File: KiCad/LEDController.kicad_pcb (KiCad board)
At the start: 4 copper layers, 90 x 90 mm, 86 parts, among them J1 UART, J10 LED2, J13 LED3, J14 LED4, J15 LED8, J16 LED7, J17 LED6, J18 LED5, J19 LED9, J20 LED10, J21 LED11, J22 LED12, J4 Conn_01x02, J5 Conn_01x02, J6 USB_C_Receptacle_USB2.0_16P, J7 Conn_01x14, J8 JTAG, J9 LED1, K1 SRD-05VDC-SL-C, Q5 AO3400A, SW1 BOOT, SW2 EN, U1 TPS54202DDC, U2 ESP32-S3-WROOM-2, U3 TPS54202DDC, U7 SN74LVC8T245, U8 SN74LVC8T245

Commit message: arrange components
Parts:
- J10, J13, J14, J15, J16, J17, J18, J19, J20, J21, J22, J9: footprint TerminalBlock_Phoenix:TerminalBlock_Phoenix_MKDS-3-3-5.08_1x03_P5.08mm_Horizontal -> Library:CONN-TH_3P-P5.08_WJ2EDGRC-5.08-3P
- J4: value Conn_01x02 -> 5V; footprint TerminalBlock_Phoenix:TerminalBlock_Phoenix_MKDS-3-2-5.08_1x02_P5.08mm_Horizontal -> Library:CONN-TH_HB9500M-9.5-2P
- J5: value Conn_01x02 -> 24V; footprint TerminalBlock_Phoenix:TerminalBlock_Phoenix_MKDS-3-2-5.08_1x02_P5.08mm_Horizontal -> Library:CONN-TH_HB9500M-9.5-2P
- moved H2 113.6 mm to (127.0, 52.0)
- moved D3 69.8 mm to (173.8, 86.0)
- moved R13 69.8 mm to (174.0, 80.0)
- moved R14 69.8 mm to (174.0, 83.0)
- moved H1 62.9 mm to (48.0, 52.0)
- moved J6 62.6 mm to (105.0, 52.7)
- moved C22 49.7 mm to (85.4, 136.8)
- moved C23 49.7 mm to (79.4, 136.8)
- moved C24 49.7 mm to (89.9, 122.8)
- moved C25 49.7 mm to (95.9, 122.8)
- moved R35 49.7 mm to (75.4, 136.3)
- moved R36 49.7 mm to (75.4, 134.3)
- moved R37 49.7 mm to (75.4, 132.3)
- moved R38 49.7 mm to (75.4, 130.3)
- moved R39 49.7 mm to (75.4, 128.3)
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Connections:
- D3 pad 1: +24V -> +5V
- J4 pad 1: +24V -> +5V
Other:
- board size 90 x 90 mm -> 85 x 110 mm
- board text removed: "-"
- board text removed: "RX"
- board text removed: "TX"

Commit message: arrange  components
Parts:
- removed J21: LED11, Library:CONN-TH_3P-P5.08_WJ2EDGRC-5.08-3P
- removed J22: LED12, Library:CONN-TH_3P-P5.08_WJ2EDGRC-5.08-3P
- removed R45, R46: 100, Resistor_SMD:R_0805_2012Metric_Pad1.20x1.40mm_HandSolder
- moved D1 51.8 mm to (209.4, 57.8)
- moved R5 51.7 mm to (204.9, 58.0), turned to 0 degrees
- moved R8 48.3 mm to (204.9, 63.9)
- moved R6 48.2 mm to (204.9, 60.9), turned to 0 degrees
- moved J20 32.2 mm to (119.5, 88.1)
- moved J19 30.8 mm to (119.5, 107.0)
- moved R35 28.5 mm to (99.8, 121.5), turned to 0 degrees
- moved J7 26.8 mm to (179.8, 58.8)
- moved R36 26.7 mm to (99.8, 123.5), turned to 0 degrees
- moved C21 26.6 mm to (95.2, 104.6), turned to 180 degrees
- moved R37 25.3 mm to (99.8, 125.5), turned to 0 degrees
- moved R12 24.8 mm to (108.8, 78.1), turned to 0 degrees
- moved J15 23.1 mm to (119.5, 126.0), turned to 90 degrees
- moved R11 21.3 mm to (104.7, 78.1), turned to 0 degrees
- moved R20 21.0 mm to (104.8, 94.5), turned to 0 degrees
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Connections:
- R35 pad 1: Net-(U7-B1) -> Net-(U8-B6)
- R35 pad 2: DataOut1 -> DataOut8
- R36 pad 1: Net-(U7-B2) -> Net-(U8-B7)
- R36 pad 2: DataOut2 -> DataOut7
- R37 pad 1: Net-(U7-B3) -> Net-(U8-B8)
- R37 pad 2: DataOut3 -> DataOut6
- R38 pad 2: DataOut4 -> DataOut5
- R39 pad 2: DataOut5 -> DataOut4
- R40 pad 2: DataOut6 -> DataOut3
- R41 pad 2: DataOut7 -> DataOut2
- R42 pad 2: DataOut8 -> DataOut1
- R43 pad 1: Net-(U8-B1) -> Net-(U8-B5)
- R44 pad 1: Net-(U8-B2) -> Net-(U8-B4)
- U7 pad 10: Data8 -> Data1
- U7 pad 19: Net-(U7-B3) -> unconnected-(U7-B3-Pad19)
- U7 pad 20: Net-(U7-B2) -> unconnected-(U7-B2-Pad20)
- U7 pad 21: Net-(U7-B1) -> unconnected-(U7-B1-Pad21)
- U7 pad 3: Data1 -> unconnected-(U7-A1-Pad3)
- U7 pad 4: Data2 -> unconnected-(U7-A2-Pad4)
- U7 pad 5: Data3 -> unconnected-(U7-A3-Pad5)
- U7 pad 6: Data4 -> Data5
- U7 pad 7: Data5 -> Data4
- U7 pad 8: Data6 -> Data3
- U7 pad 9: Data7 -> Data2
- U8 pad 10: unconnected-(U8-A8-Pad10) -> Data6
- U8 pad 14: unconnected-(U8-B8-Pad14) -> Net-(U8-B8)
- U8 pad 15: unconnected-(U8-B7-Pad15) -> Net-(U8-B7)
- U8 pad 16: unconnected-(U8-B6-Pad16) -> Net-(U8-B6)
- U8 pad 17: unconnected-(U8-B5-Pad17) -> Net-(U8-B5)
- U8 pad 19: Net-(U8-B3) -> unconnected-(U8-B3-Pad19)
- U8 pad 20: Net-(U8-B2) -> unconnected-(U8-B2-Pad20)
- U8 pad 21: Net-(U8-B1) -> unconnected-(U8-B1-Pad21)
- U8 pad 3: Data9 -> unconnected-(U8-A1-Pad3)
- U8 pad 4: Data10 -> unconnected-(U8-A2-Pad4)
- U8 pad 5: Data11 -> unconnected-(U8-A3-Pad5)
- U8 pad 6: Data12 -> Data10
- U8 pad 7: unconnected-(U8-A5-Pad7) -> Data9
- U8 pad 8: unconnected-(U8-A6-Pad8) -> Data8
- U8 pad 9: unconnected-(U8-A7-Pad9) -> Data7
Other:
- board size 85 x 110 mm -> 85 x 100 mm
- board text removed: "3V3"
- board text removed: "G11"
- board text removed: "G12"
- board text removed: "G13"
- board text removed: "G14"
- board text removed: "G17"
- board text removed: "G18"
- board text removed: "G21"
- board text removed: "G38"
- board text removed: "G45"
- board text removed: "G46"
- board text removed: "G47"
- board text removed: "G8"
- board text removed: "GND"

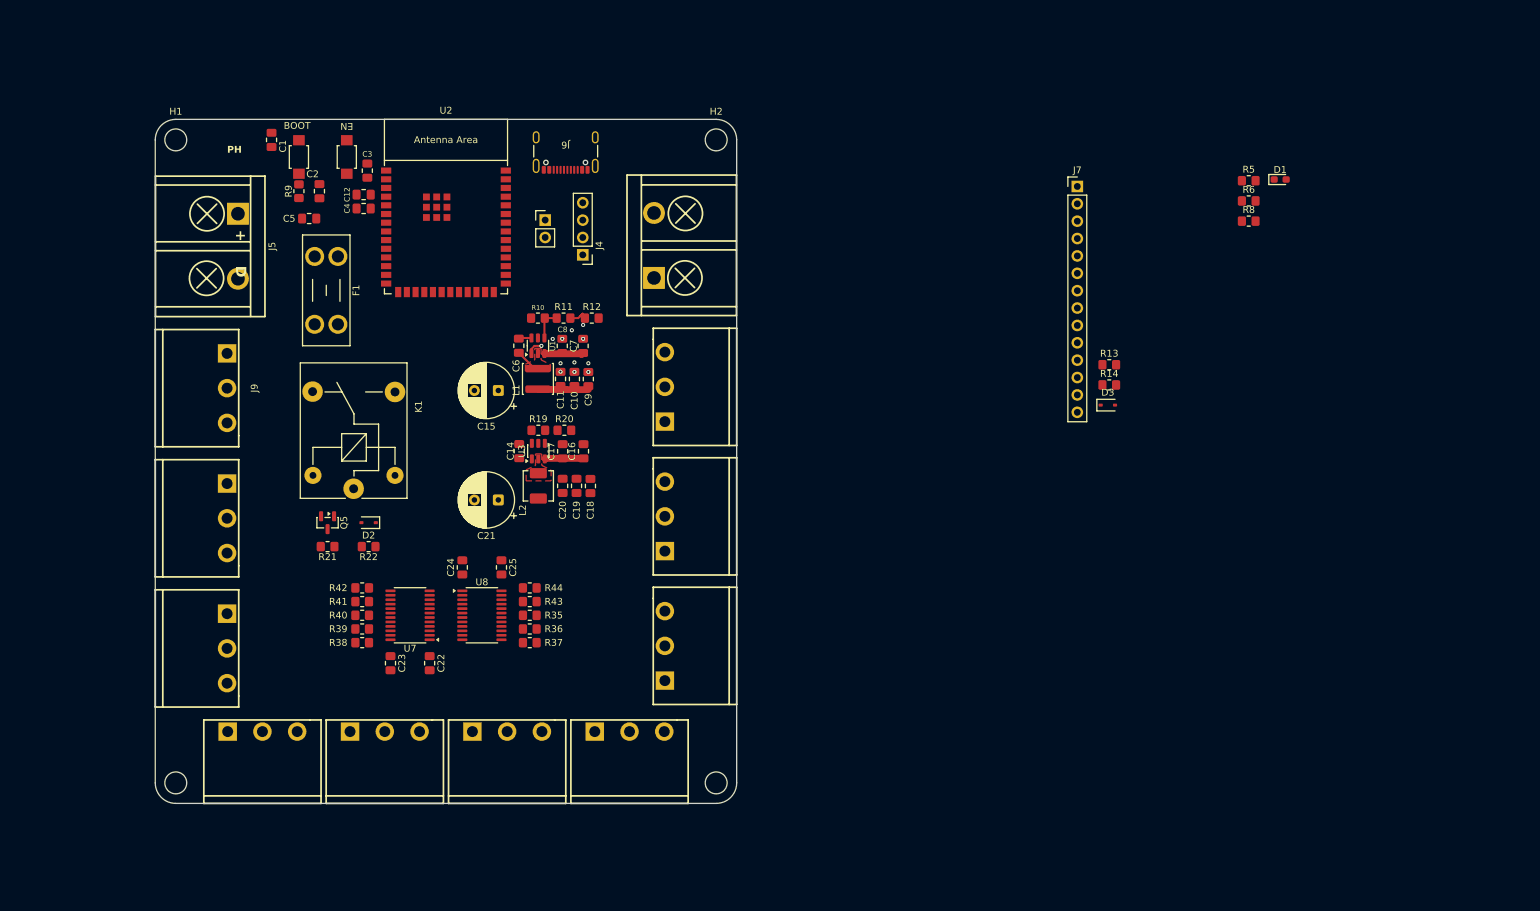
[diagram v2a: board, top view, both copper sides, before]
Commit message: add ideal diode
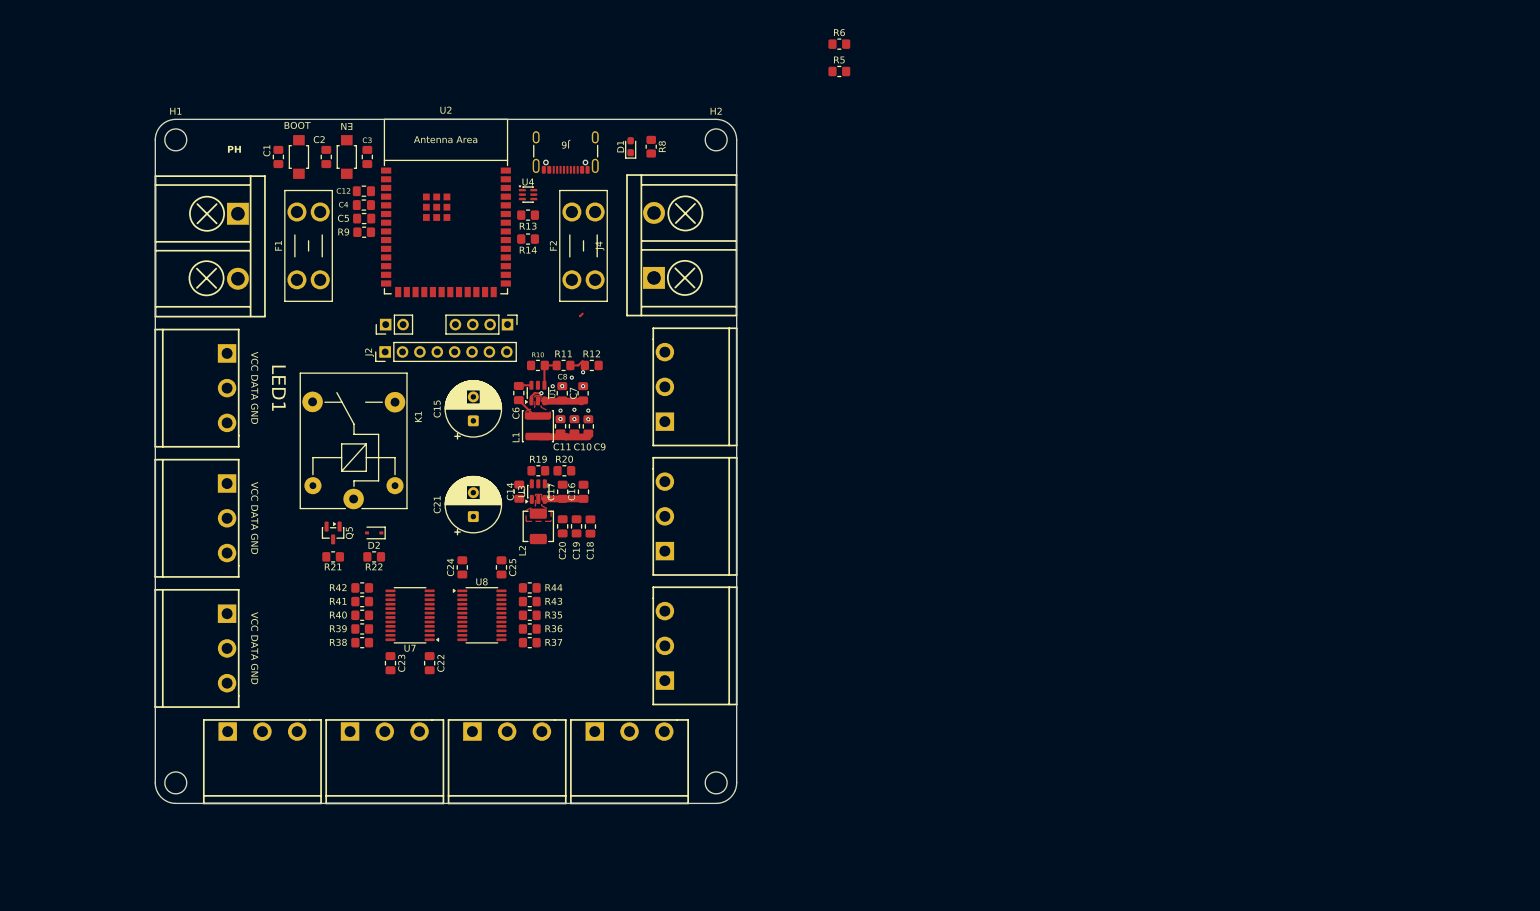
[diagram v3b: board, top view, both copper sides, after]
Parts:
- removed D3: 1N4148WS, Diode_SMD:D_SOD-323
- removed J7: Conn_01x14, Connector_PinHeader_2.54mm:PinHeader_1x14_P2.54mm_Vertical
- added F2: Fuse, Fuse:Fuseholder_Blade_Mini_Keystone_3568, F.Cu at (105.9, 72.5)
- added J2: Conn_01x08, Connector_PinHeader_2.54mm:PinHeader_1x08_P2.54mm_Vertical, F.Cu at (78.6, 83.0)
- added U4: LM66100DCK, Package_TO_SOT_SMD:SOT-363_SC-70-6, F.Cu at (99.5, 60.0)
- moved D1 95.1 mm to (114.5, 53.0), turned to 90 degrees
- moved R8 88.0 mm to (117.5, 53.0), turned to -90 degrees
- moved R13 87.7 mm to (99.5, 63.0), turned to 180 degrees
- moved R14 87.6 mm to (99.5, 66.5), turned to 180 degrees
- moved R6 64.1 mm to (145.0, 38.0)
- moved R5 62.0 mm to (145.0, 42.0)
- moved J1 27.9 mm to (78.7, 79.0), turned to 90 degrees
- moved J8 15.0 mm to (96.5, 79.0), turned to -90 degrees
- moved R9 11.3 mm to (75.5, 65.5), turned to 0 degrees
- moved C5 8.04 mm to (75.5, 63.5)
- moved C10 6.92 mm to (106.3, 93.9)
- moved C11 6.92 mm to (104.2, 93.9)
- moved C9 6.92 mm to (108.3, 93.9)
- moved L1 6.92 mm to (100.9, 93.9)
- moved R10 6.92 mm to (100.9, 85.0)
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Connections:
- F1 pad 2: Net-(F1-Pad2) -> Net-(J5-Pin_1)
- J4 pad 1: +5V -> Net-(J4-Pin_1)
- J5 pad 1: +24V -> Net-(J5-Pin_1)
- K1 pad 1: Net-(F1-Pad2) -> +24V
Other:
- board text added: "LED1"
- board text added: "VCC DATA GND"
- board text removed: "+"
- board text removed: "D"

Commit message: add esd protection, pullup on EN, Replicate layout
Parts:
- removed L1: 10u, Inductor_SMD:L_APV_ANR4026
- added C26: 220uF, Capacitor_THT:CP_Radial_D8.0mm_P3.50mm, F.Cu at (103.3, 93.0)
- added C27: 75p, Capacitor_SMD:C_0805_2012Metric_Pad1.18x1.45mm_HandSolder, F.Cu at (83.2, 111.0)
- added J3: Power over USB, Connector_PinHeader_2.54mm:PinHeader_1x02_P2.54mm_Vertical, F.Cu at (106.7, 84.5)
- added L3: 15u, Inductor_SMD:L_APV_APH0630, F.Cu at (96.0, 97.5)
- added R15: 22, Resistor_SMD:R_0805_2012Metric_Pad1.20x1.40mm_HandSolder, F.Cu at (75.5, 71.5)
- added R7: 22, Resistor_SMD:R_0805_2012Metric_Pad1.20x1.40mm_HandSolder, F.Cu at (75.5, 73.5)
- added U5: USBLC6-2SC6, Package_TO_SOT_SMD:SOT-23-6, F.Cu at (100.5, 61.0)
- C15: value 220uF -> 56p; footprint Capacitor_THT:CP_Radial_D8.0mm_P3.50mm -> Capacitor_SMD:C_0805_2012Metric_Pad1.18x1.45mm_HandSolder
- L2: footprint Inductor_SMD:L_APV_APH0420 -> Inductor_SMD:L_APV_APH0630
- R11: value 1.8k -> 10k
- R12: value 20k -> 22k
- moved R8 53.4 mm to (71.8, 80.5)
- moved D1 52.5 mm to (69.8, 80.5)
- moved R12 24.6 mm to (85.5, 92.8), turned to 90 degrees
- moved R14 21.7 mm to (116.5, 53.0), turned to -90 degrees
- moved R20 20.2 mm to (85.5, 106.3), turned to 90 degrees
- moved R10 19.9 mm to (85.5, 97.5), turned to 90 degrees
- moved R19 18.8 mm to (85.5, 111.0), turned to 90 degrees
- moved C7 18.7 mm to (89.0, 91.8), turned to 180 degrees
- moved C16 18.7 mm to (89.0, 105.3), turned to 180 degrees
- moved R13 17.8 mm to (114.2, 53.0), turned to -90 degrees
- moved C8 16.2 mm to (89.0, 93.9), turned to 180 degrees
- moved C17 16.0 mm to (89.0, 107.4), turned to 180 degrees
- moved C18 15.7 mm to (93.8, 103.3), turned to 180 degrees
- moved C6 15.0 mm to (89.0, 100.8), turned to 180 degrees
- moved U1 14.7 mm to (89.0, 97.5), turned to 180 degrees
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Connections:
- net +24V renamed VCC_IN
- net +24V_SW renamed VCC_SW
- C15 pad 2: GND -> Net-(U1-FB)
- J6 pad A6: USB.D+ -> Net-(J6-D+-PadA6)
- J6 pad A7: USB.D- -> Net-(J6-D--PadA7)
- J6 pad B6: USB.D+ -> Net-(J6-D+-PadA6)
- J6 pad B7: USB.D- -> Net-(J6-D--PadA7)
- R11 pad 1: Net-(U1-FB) -> +3.3V
- R11 pad 2: Net-(R11-Pad2) -> ESP_BOOT
- R12 pad 1: Net-(R11-Pad2) -> Net-(U1-FB)
- R13 pad 1: Net-(J6-CC1) -> GND
- R13 pad 2: GND -> Net-(J6-CC2)
- R14 pad 1: Net-(J6-CC2) -> GND
- R14 pad 2: GND -> Net-(J6-CC1)
- R35 pad 1: Net-(U8-B6) -> Net-(U8-B4)
- R36 pad 1: Net-(U8-B7) -> Net-(U8-B6)
- R38 pad 1: Net-(U7-B4) -> Net-(U7-B1)
- R39 pad 1: Net-(U7-B5) -> Net-(U7-B3)
- R40 pad 1: Net-(U7-B6) -> Net-(U7-B5)
- R43 pad 1: Net-(U8-B5) -> Net-(U8-B2)
- R44 pad 1: Net-(U8-B4) -> Net-(U8-B1)
- U2 pad 13: USB.D- -> Net-(U2-GPIO19/U1RTS/ADC2_CH8/CLK_OUT2/USB_D-)
- U2 pad 14: USB.D+ -> Net-(U2-GPIO20/U1CTS/ADC2_CH9/CLK_OUT1/USB_D+)
- U7 pad 16: Net-(U7-B6) -> unconnected-(U7-B6-Pad16)
- U7 pad 18: Net-(U7-B4) -> unconnected-(U7-B4-Pad18)
- U7 pad 19: unconnected-(U7-B3-Pad19) -> Net-(U7-B3)
- U7 pad 21: unconnected-(U7-B1-Pad21) -> Net-(U7-B1)
- U7 pad 3: unconnected-(U7-A1-Pad3) -> Data5
- U7 pad 5: unconnected-(U7-A3-Pad5) -> Data4
- U7 pad 6: Data5 -> unconnected-(U7-A4-Pad6)
- U7 pad 7: Data4 -> Data3
- U7 pad 8: Data3 -> unconnected-(U7-A6-Pad8)
- U8 pad 15: Net-(U8-B7) -> unconnected-(U8-B7-Pad15)
- U8 pad 17: Net-(U8-B5) -> unconnected-(U8-B5-Pad17)
- U8 pad 20: unconnected-(U8-B2-Pad20) -> Net-(U8-B2)
- U8 pad 21: unconnected-(U8-B1-Pad21) -> Net-(U8-B1)
- U8 pad 3: unconnected-(U8-A1-Pad3) -> Data10
- U8 pad 4: unconnected-(U8-A2-Pad4) -> Data9
- U8 pad 6: Data10 -> Data8
- U8 pad 7: Data9 -> unconnected-(U8-A5-Pad7)
- U8 pad 8: Data8 -> Data7
- U8 pad 9: Data7 -> unconnected-(U8-A7-Pad9)
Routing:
- net +5V: track 0.00 -> 14.5 mm
- net VCC_IN: track 12.1 -> 4.21 mm
- net Net-(U3-FB): track 0.00 -> 7.31 mm
- net +3.3V: track 7.31 -> 14.5 mm
- net Net-(U3-SW): track 0.00 -> 4.57 mm
- net Net-(U1-FB): track 4.60 -> 7.31 mm
- net Net-(R11-Pad2): track 2.59 -> 0.00 mm
- net Net-(U3-BOOT): track 0.00 -> 2.43 mm
- net GND: track 2.31 -> 0.00 mm, vias 12 -> 0
- net Net-(U1-SW): track 3.24 -> 4.57 mm
- net Net-(U1-BOOT): track 1.74 -> 2.43 mm
- added copper zone on F.Cu, net GND
- added copper zone on In1.Cu, net GND
- added copper zone on In2.Cu, net GND
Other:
- board text added: "Close for Power over USB Open for ext. PSU"
- board text added: "LED2"
- board text added: "LED3"
- board text added: "LED4"
- board text added: "LED5"
- board text added: "LED6"
- board text added: "LED7"

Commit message: cleanup kicad folder
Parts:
- moved R6 57.9 mm to (100.5, 75.0), turned to 180 degrees
- moved R5 56.6 mm to (100.5, 77.0), turned to 180 degrees
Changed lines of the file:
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@@
 	(footprint "Resistor_SMD:R_0805_2012Metric_Pad1.20x1.40mm_HandSolder"
 		(layer "F.Cu")
-		(at 145 38)
+		(at 100.5 75 180)
 		(descr "Resistor SMD 0805 (2012 Metric), square (rectangular) end terminal, IPC-7351 nominal with elongated pad for handsoldering. (Body size source: IPC-SM-782 page 72, https://www.pcb-3d.com/wordpress/wp-content/uploads/ipc-sm-782a_amendment_1_and_2.pdf)")
 		(tags "resistor handsolder")
@@
 		)
 		(property "LCSC" "C2930231"
-			(at 0 0 0)
+			(at 0 0 180)
 			(unlocked yes)
 			(layer "F.Fab")
@@
 		(duplicate_pad_numbers_are_jumpers no)
 		(fp_line
-			(start -0.227064 -0.735)
-			(end 0.227064 -0.735)
+			(start -0.227064 0.735)
+			(end 0.227064 0.735)
 			(stroke
 				(width 0.12)
@@
 		)
 		(fp_line
-			(start -0.227064 0.735)
-			(end 0.227064 0.735)
+			(start -0.227064 -0.735)
+			(end 0.227064 -0.735)
 			(stroke
 				(width 0.12)
@@
 		)
 		(pad "1" smd roundrect
-			(at -1 0)
+			(at -1 0 180)
 			(size 1.2 1.4)
 			(layers "F.Cu" "F.Mask" "F.Paste")
@@
 		)
 		(pad "2" smd roundrect
-			(at 1 0)
+			(at 1 0 180)
 			(size 1.2 1.4)
 			(layers "F.Cu" "F.Mask" "F.Paste")
@@
 	(footprint "Resistor_SMD:R_0805_2012Metric_Pad1.20x1.40mm_HandSolder"
 		(layer "F.Cu")
-		(at 145 42)
+		(at 100.5 77 180)
 		(descr "Resistor SMD 0805 (2012 Metric), square (rectangular) end terminal, IPC-7351 nominal with elongated pad for handsoldering. (Body size source: IPC-SM-782 page 72, https://www.pcb-3d.com/wordpress/wp-content/uploads/ipc-sm-782a_amendment_1_and_2.pdf)")
 		(tags "resistor handsolder")
@@
 		)
 		(property "LCSC" "C2930231"
-			(at 0 0 0)
+			(at 0 0 180)
 			(unlocked yes)
 			(layer "F.Fab")
@@
 		(duplicate_pad_numbers_are_jumpers no)
 		(fp_line
-			(start -0.227064 -0.735)
-			(end 0.227064 -0.735)
+			(start -0.227064 0.735)
+			(end 0.227064 0.735)
 			(stroke
 				(width 0.12)
@@
 		)
 		(fp_line
-			(start -0.227064 0.735)
-			(end 0.227064 0.735)
+			(start -0.227064 -0.735)
+			(end 0.227064 -0.735)
 			(stroke
 				(width 0.12)
@@
 		)
 		(pad "1" smd roundrect
-			(at -1 0)
+			(at -1 0 180)
 			(size 1.2 1.4)
 			(layers "F.Cu" "F.Mask" "F.Paste")
@@
 		)
 		(pad "2" smd roundrect
-			(at 1 0)
+			(at 1 0 180)
 			(size 1.2 1.4)
 			(layers "F.Cu" "F.Mask" "F.Paste")
@@
 	)
 	(segment
-		(start 92.975 97.925)
-		(end 92.975 97.5)
-		(width 0.3)
-		(layer "F.Cu")
-		(net "Net-(U1-SW)")
-	)
-	(segment
-		(start 90.0375 100.837158)
-		(end 90.062842 100.837158)
-		(width 0.3)
-		(layer "F.Cu")
-		(net "Net-(U1-SW)")
-	)
-	(segment
-		(start 90.062842 100.837158)
-		(end 92.975 97.925)
-		(width 0.3)
-		(layer "F.Cu")
-		(net "Net-(U1-SW)")
-	)
-	(segment
 		(start 83.25 96.4625)
 		(end 85.4225 96.4625)
@@
 	)
 	(segment
+		(start 92.975 97.925)
+		(end 92.975 97.5)
+		(width 0.3)
+		(layer "F.Cu")
+		(net "Net-(U1-SW)")
+	)
+	(segment
+		(start 90.0375 100.837158)
+		(end 90.062842 100.837158)
+		(width 0.3)
+		(layer "F.Cu")
+		(net "Net-(U1-SW)")
+	)
+	(segment
+		(start 90.062842 100.837158)
+		(end 92.975 97.925)
+		(width 0.3)
+		(layer "F.Cu")
+		(net "Net-(U1-SW)")
+	)
+	(segment
+		(start 90.0615 107.444)
+		(end 90.0615 105.337158)
+		(width 1)
+		(layer "F.Cu")
+		(net "VCC_IN")
+	)
+	(segment
+		(start 90.0615 93.944)
+		(end 90.0615 91.837158)
+		(width 1)
+		(layer "F.Cu")
+		(net "VCC_IN")
+	)
+	(segment
 		(start 87.8625 100.737158)
 		(end 87.9625 100.837158)
@@
 		(net "Net-(U3-BOOT)")
 	)
-	(segment
-		(start 90.0615 107.444)
-		(end 90.0615 105.337158)
-		(width 1)
-		(layer "F.Cu")
-		(net "VCC_IN")
-	)
-	(segment
-		(start 90.0615 93.944)
-		(end 90.0615 91.837158)
-		(width 1)
-		(layer "F.Cu")
-		(net "VCC_IN")
-	)
 	(zone

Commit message: .
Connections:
- R8 pad 2: GPIO.6 -> GPIO.18
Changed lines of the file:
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@@
 			(layers "F.Cu" "F.Mask" "F.Paste")
 			(roundrect_rratio 0.208333)
-			(net "GPIO.6")
+			(net "GPIO.18")
 			(pintype "passive")
 		)
